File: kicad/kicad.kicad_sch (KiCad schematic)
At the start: 20 parts, among them J1 DEBUG_LED_CONN, J101 EPD_SPI_CONN, J102 HPC_CONN, J103 GLOBAL_CONN, J105 INPUT_CONN, J106 STORAGE_CONN, J107 USBC_CONN

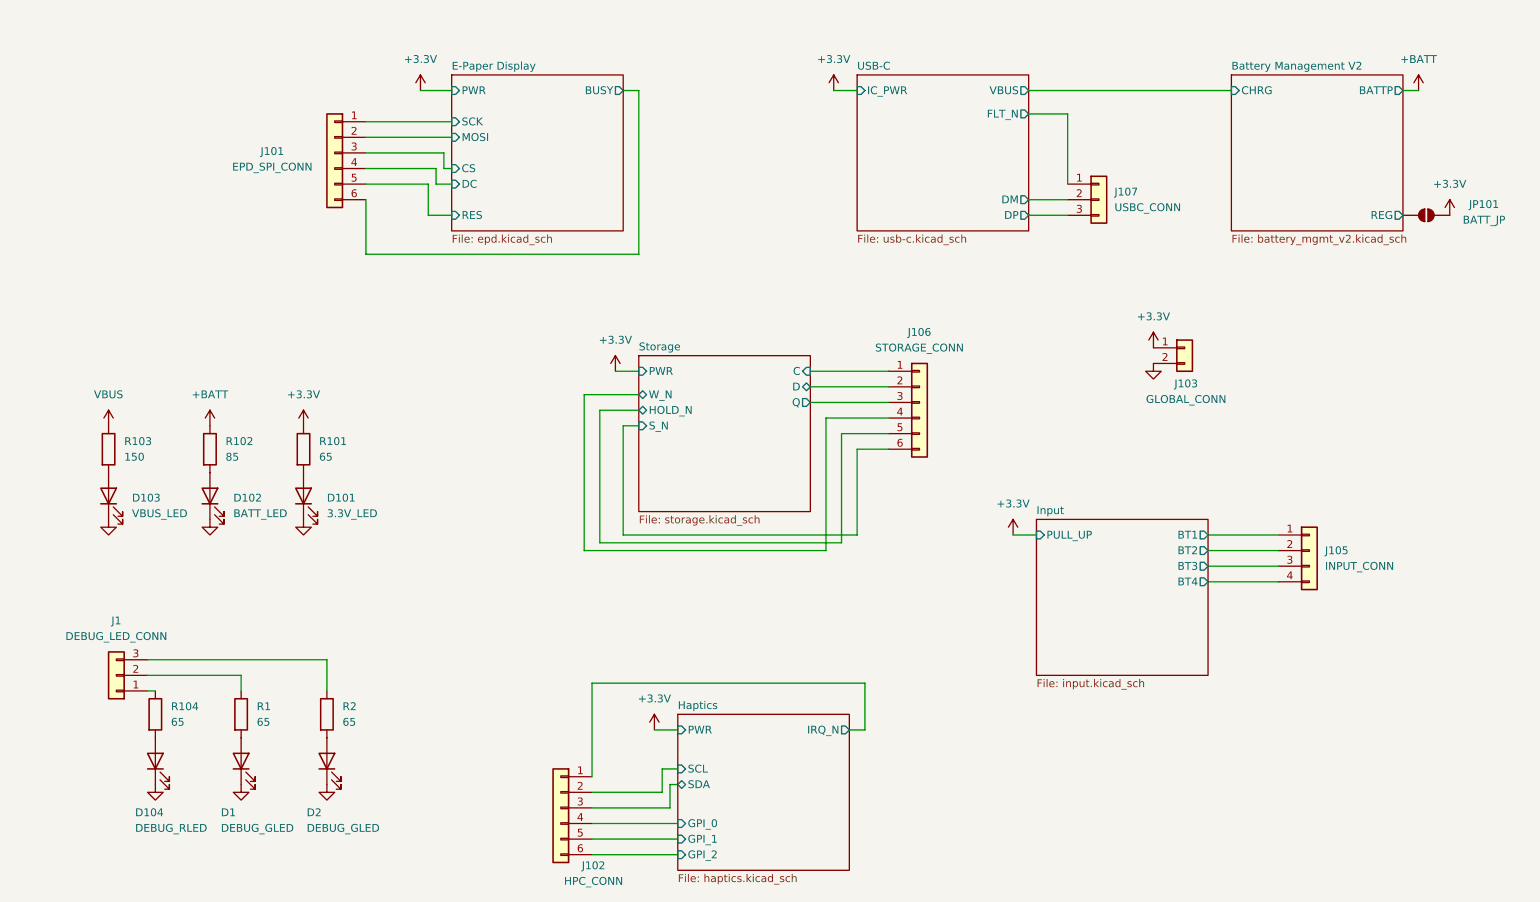
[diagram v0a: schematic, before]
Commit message: essentially finish schematic, start adding footprints, add new footprints
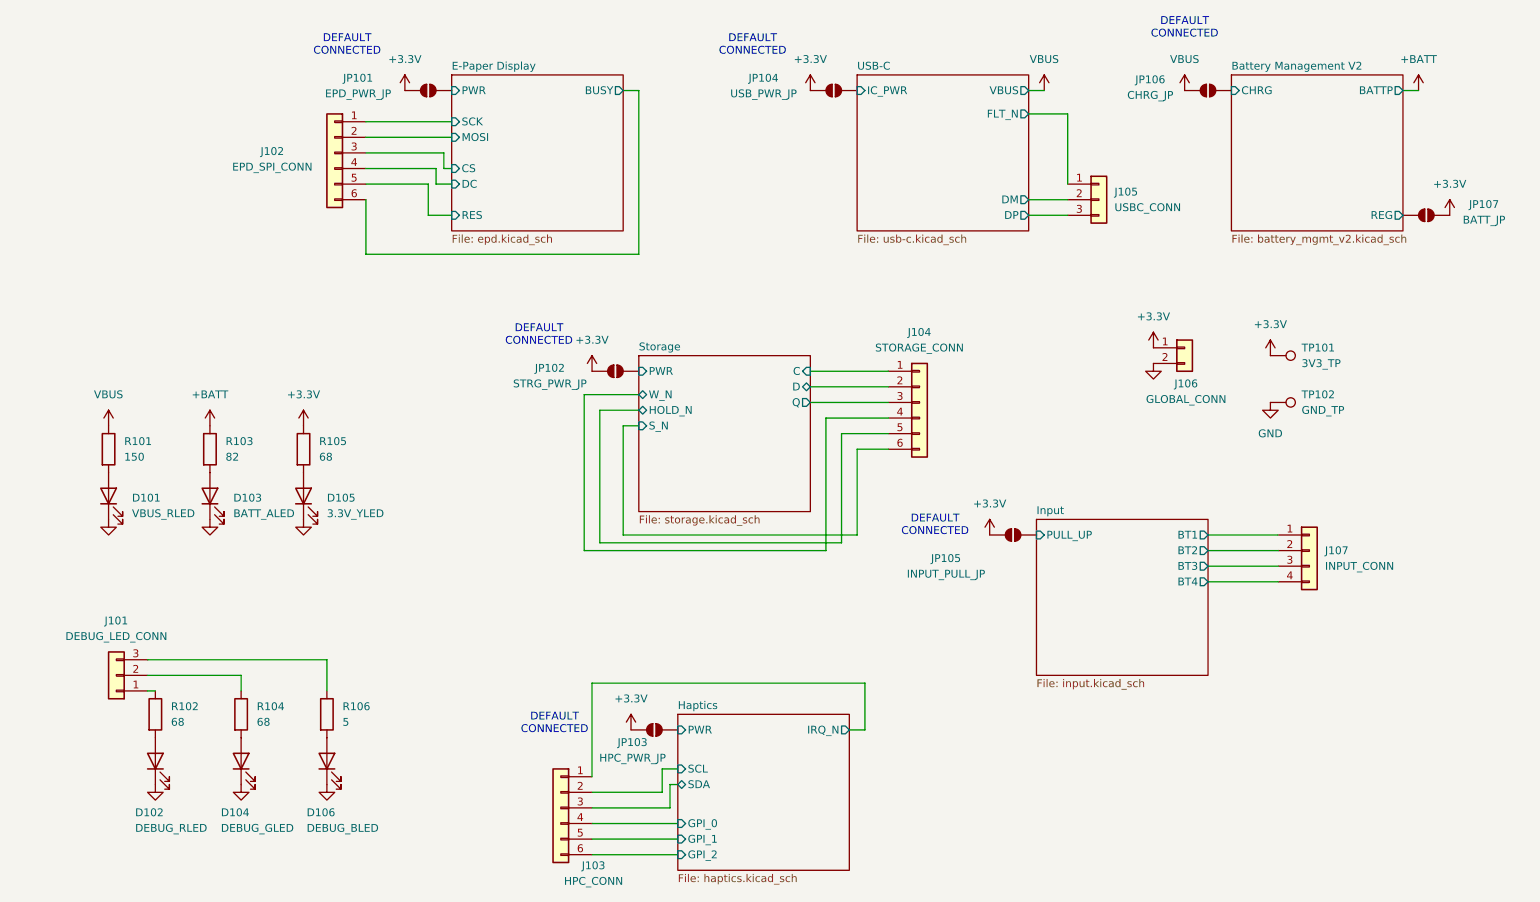
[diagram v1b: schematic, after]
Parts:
- added JP101: EPD_PWR_JP, Jumper:SolderJumper-2_P1.3mm_Open_TrianglePad1.0x1.5mm, symbol Jumper:SolderJumper_2_Open
- added JP102: STRG_PWR_JP, Jumper:SolderJumper-2_P1.3mm_Open_TrianglePad1.0x1.5mm, symbol Jumper:SolderJumper_2_Open
- added JP103: HPC_PWR_JP, Jumper:SolderJumper-2_P1.3mm_Open_TrianglePad1.0x1.5mm, symbol Jumper:SolderJumper_2_Open
- added JP104: USB_PWR_JP, Jumper:SolderJumper-2_P1.3mm_Open_TrianglePad1.0x1.5mm, symbol Jumper:SolderJumper_2_Open
- added JP105: INPUT_PULL_JP, Jumper:SolderJumper-2_P1.3mm_Open_TrianglePad1.0x1.5mm, symbol Jumper:SolderJumper_2_Open
- added JP106: CHRG_JP, Jumper:SolderJumper-2_P1.3mm_Open_TrianglePad1.0x1.5mm, symbol Jumper:SolderJumper_2_Open
- added TP101: 3V3_TP, TestPoint:TestPoint_Pad_D3.0mm, symbol Connector:TestPoint
- added TP102: GND_TP, TestPoint:TestPoint_Pad_D3.0mm, symbol Connector:TestPoint
- D101: renamed from D103; value VBUS_LED -> VBUS_RLED; footprint (none) -> Jumper:SolderJumper-3_P2.0mm_Open_TrianglePad1.0x1.5mm_NumberLabels
- D102: renamed from D104; footprint (none) -> Diode_SMD:D_0603_1608Metric_Pad1.05x0.95mm_HandSolder
- D103: renamed from D102; value BATT_LED -> BATT_ALED; footprint (none) -> Diode_SMD:D_0603_1608Metric_Pad1.05x0.95mm_HandSolder
- D104: renamed from D1; footprint (none) -> Diode_SMD:D_0603_1608Metric_Pad1.05x0.95mm_HandSolder
- D105: renamed from D101; value 3.3V_LED -> 3.3V_YLED; footprint (none) -> Diode_SMD:D_0603_1608Metric_Pad1.05x0.95mm_HandSolder
- D106: renamed from D2; value DEBUG_GLED -> DEBUG_BLED; footprint (none) -> Diode_SMD:D_0603_1608Metric_Pad1.05x0.95mm_HandSolder
- J101: renamed from J1; footprint (none) -> Connector_JST:JST_XH_B3B-XH-A_1x03_P2.50mm_Vertical
- J102: renamed from J101; footprint (none) -> Connector_JST:JST_XH_B6B-XH-A_1x06_P2.50mm_Vertical
- J103: renamed from J102; footprint (none) -> Connector_JST:JST_XH_B6B-XH-A_1x06_P2.50mm_Vertical
- J104: renamed from J106; footprint (none) -> Connector_JST:JST_XH_B6B-XH-A_1x06_P2.50mm_Vertical
- J105: renamed from J107; footprint (none) -> Connector_JST:JST_XH_B3B-XH-A_1x03_P2.50mm_Vertical
- J106: renamed from J103; footprint (none) -> Connector_JST:JST_XH_B2B-XH-A_1x02_P2.50mm_Vertical
- J107: renamed from J105; footprint (none) -> Connector_JST:JST_XH_B4B-XH-A_1x04_P2.50mm_Vertical
- JP107: renamed from JP101; footprint (none) -> Jumper:SolderJumper-2_P1.3mm_Open_TrianglePad1.0x1.5mm
- R101: renamed from R103; footprint (none) -> Resistor_SMD:R_0603_1608Metric_Pad0.98x0.95mm_HandSolder
- R102: renamed from R104; value 65 -> 68; footprint (none) -> Resistor_SMD:R_0603_1608Metric_Pad0.98x0.95mm_HandSolder
- R103: renamed from R102; value 85 -> 82; footprint (none) -> Resistor_SMD:R_0603_1608Metric_Pad0.98x0.95mm_HandSolder
- R104: renamed from R1; value 65 -> 68; footprint (none) -> Resistor_SMD:R_0603_1608Metric_Pad0.98x0.95mm_HandSolder
- R105: renamed from R101; value 65 -> 68; footprint (none) -> Resistor_SMD:R_0603_1608Metric_Pad0.98x0.95mm_HandSolder
- R106: renamed from R2; value 65 -> 5; footprint (none) -> Resistor_SMD:R_0603_1608Metric_Pad0.98x0.95mm_HandSolder
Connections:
- net +3.3V: now also JP101.1 (A), JP102.1 (A), JP103.1 (A), JP104.1 (A), JP105.1 (A), TP101.1
- net Battery Management V2/CHRG: now also JP106.1 (A)
- net GND: now also TP102.1
- net VBUS: now also JP106.2 (B)
- new net E-Paper Display/PWR: JP101.2 (B)
- new net Haptics/PWR: JP103.2 (B)
- new net Input/PULL_UP: JP105.2 (B)
- new net Storage/PWR: JP102.2 (B)
- new net USB-C/IC_PWR: JP104.2 (B)
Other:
- note added: "DEFAULT CONNECTED"

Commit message: fix motor with spring fingers, start PCB
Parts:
- D101: footprint Jumper:SolderJumper-3_P2.0mm_Open_TrianglePad1.0x1.5mm_NumberLabels -> Diode_SMD:D_0603_1608Metric_Pad1.05x0.95mm_HandSolder
- TP101, TP102: footprint TestPoint:TestPoint_Pad_D3.0mm -> TestPoint:TestPoint_Pad_D1.5mm
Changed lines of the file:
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@@
 			)
 		)
-		(property "Footprint" "Jumper:SolderJumper-3_P2.0mm_Open_TrianglePad1.0x1.5mm_NumberLabels"
+		(property "Footprint" "Diode_SMD:D_0603_1608Metric_Pad1.05x0.95mm_HandSolder"
 			(at 31.75 111.76 0)
 			(effects
@@
 			)
 		)
-		(property "Footprint" "TestPoint:TestPoint_Pad_D3.0mm"
+		(property "Footprint" "TestPoint:TestPoint_Pad_D1.5mm"
 			(at 220.98 101.6 0)
 			(effects
@@
 			)
 		)
-		(property "Footprint" "TestPoint:TestPoint_Pad_D3.0mm"
+		(property "Footprint" "TestPoint:TestPoint_Pad_D1.5mm"
 			(at 220.98 93.98 0)
 			(effects

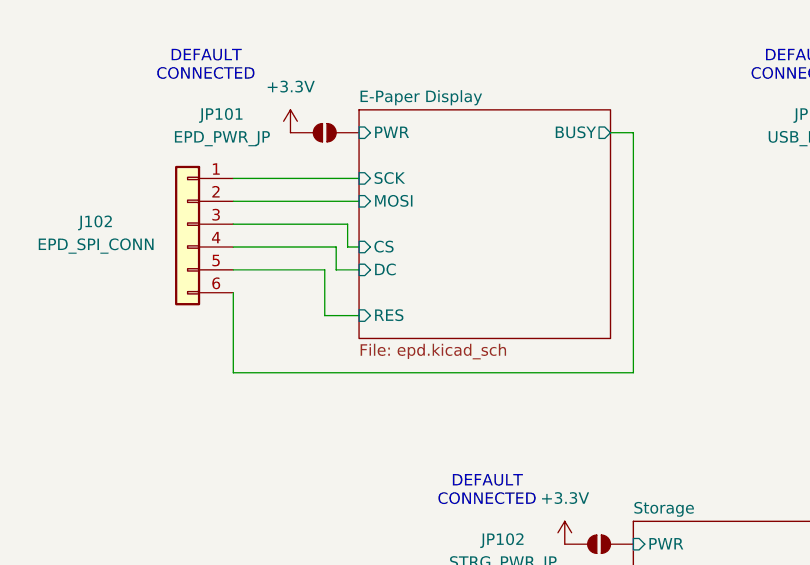
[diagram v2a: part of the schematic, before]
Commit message: PCB almost finished: only battery & usb-c needed
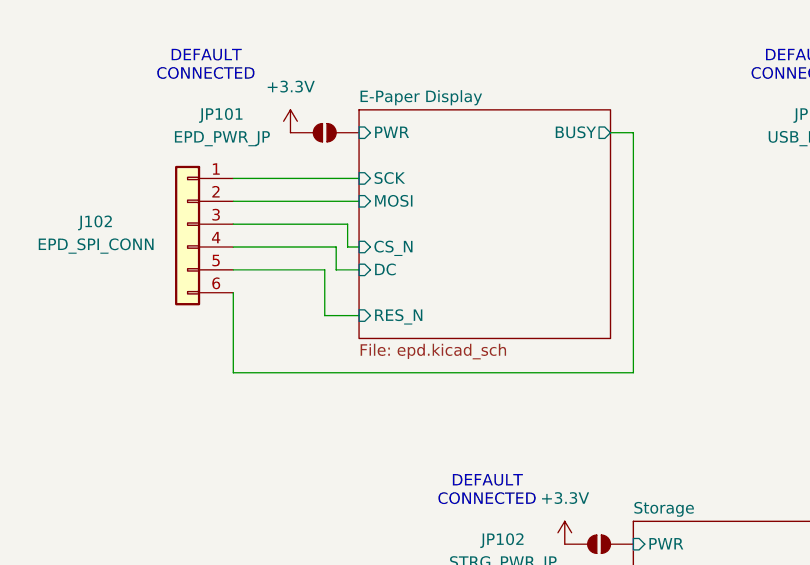
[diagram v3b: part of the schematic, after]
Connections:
- net E-Paper Display/CS renamed E-Paper Display/CS_N
- net E-Paper Display/RES renamed E-Paper Display/RES_N
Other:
- sheet E-Paper Display ports: added CS_N, RES_N; removed CS, RES
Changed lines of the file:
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@@
-			)
-		)
-		(pin "RES" input
-			(at 87.63 66.04 180)
-			(effects
-				(font
-					(size 1.27 1.27)
-				)
-				(justify left)
 			)
 		)
@@
 			)
 		)
-		(pin "CS" input
-			(at 87.63 58.42 180)
-			(effects
-				(font
-					(size 1.27 1.27)
-				)
-				(justify left)
-			)
-		)
 		(pin "SCK" input
 			(at 87.63 50.8 180)
@@
 			(effects
 				(font
+					(size 1.27 1.27)
+				)
+				(justify left)
+			)
+		)
+		(pin "RES_N" input
+			(at 87.63 66.04 180)
+			(effects
+				(font
+					(size 1.27 1.27)
+				)
+				(justify left)
+			)
+		)
+		(pin "CS_N" input
+			(at 87.63 58.42 180)
+			(effects
+				(font

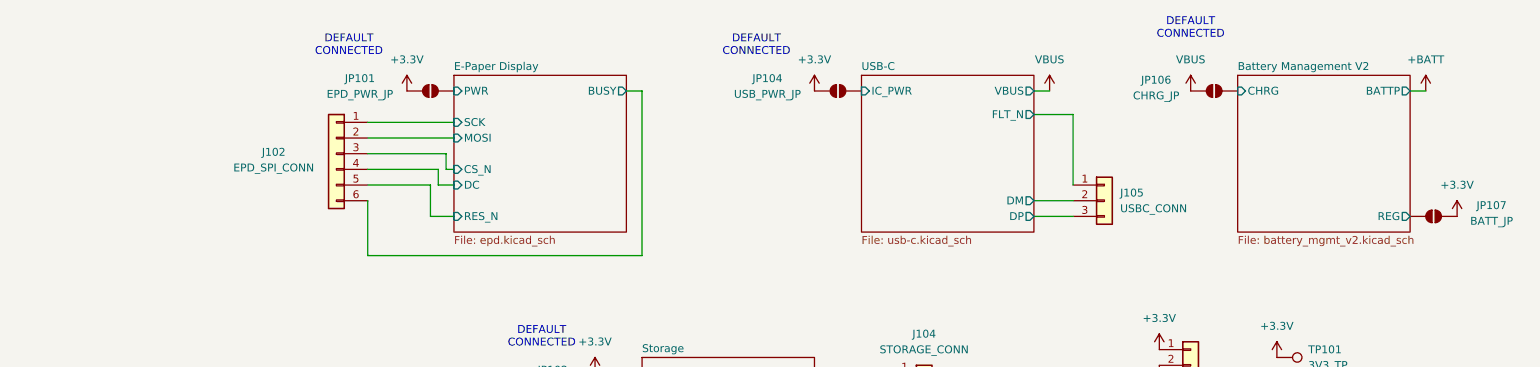
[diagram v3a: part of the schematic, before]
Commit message: finish PCB routing, need silkscreen + checks
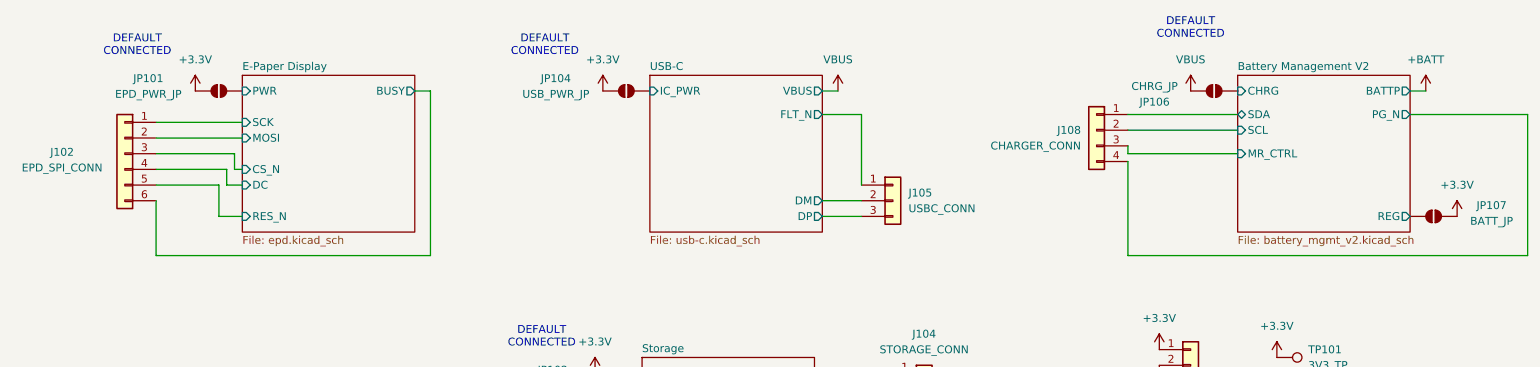
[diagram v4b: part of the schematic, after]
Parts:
- added J108: CHARGER_CONN, Connector_JST:JST_XH_B4B-XH-A_1x04_P2.50mm_Vertical, symbol Connector_Generic:Conn_01x04
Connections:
- net Battery Management V2/CHRG: now also JP106.2 (B); no longer JP106.1 (A)
- net VBUS: now also JP106.1 (A); no longer JP106.2 (B)
- new net Battery Management V2/MR_CTRL: J108.3 (Pin_3)
- new net Battery Management V2/PG_N: J108.4 (Pin_4)
- new net Battery Management V2/SCL: J108.2 (Pin_2)
- new net Battery Management V2/SDA: J108.1 (Pin_1)
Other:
- sheet Battery Management V2 ports: added MR_CTRL, PG_N, SCL, SDA; removed none
- moved on the sheet: J102, J105, JP101, JP104
